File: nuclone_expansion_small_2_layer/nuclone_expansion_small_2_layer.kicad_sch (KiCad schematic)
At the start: 44 parts, among them J3 nuclone_small_left, J4 nuclone_small_right

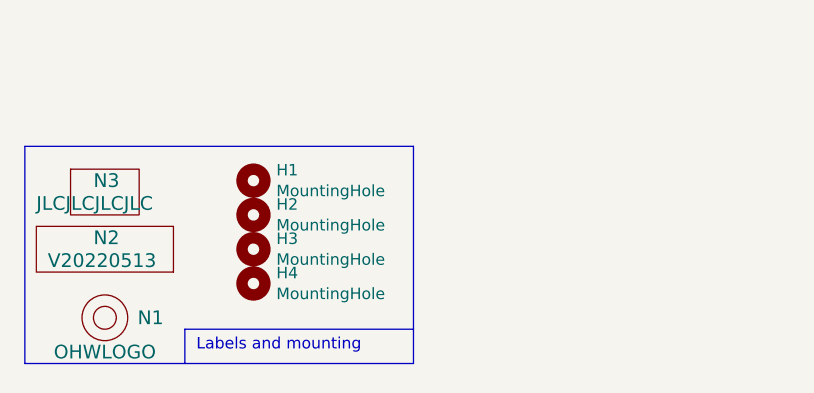
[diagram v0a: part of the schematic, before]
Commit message: updated small nuclone PCB expansion template
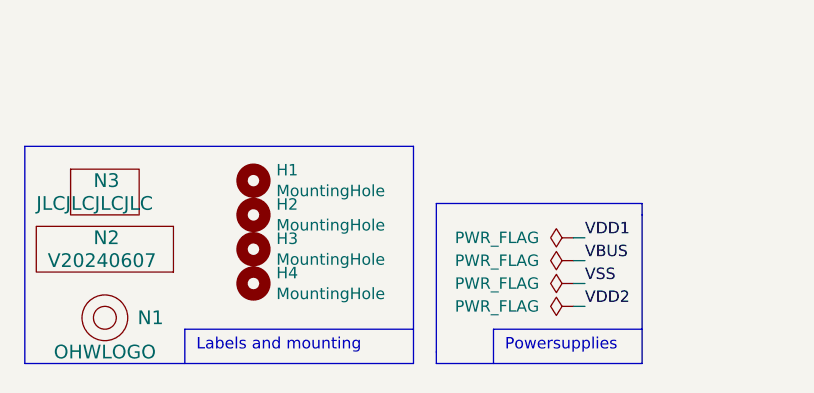
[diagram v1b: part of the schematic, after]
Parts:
- H1, H2, H3, H4: footprint MountingHole:MountingHole_3.2mm_M3_Pad_Via -> SquantorPcbOutline:MountingHole_3.2mm_M3_Pad_Via
- N1: footprint Symbols:OSHW-Symbol_6.7x6mm_SilkScreen -> Symbol:OSHW-Symbol_6.7x6mm_SilkScreen
- N2: value V20220513 -> V20240607
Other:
- note added: "Powersupplies"
